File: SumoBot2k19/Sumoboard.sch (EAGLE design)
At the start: 38 parts

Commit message: rerouting
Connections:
- removed net VDD: FL_TOF.7, FR_TOF.7, F_TOF.7, L_TOF.7, R_TOF.7
- net FR_REF: now also B1.A1/15; no longer B1.A6/20*
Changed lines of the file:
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@@
-</segment>
-</net>
-<net name="VDD" class="0">
-<segment>
-<pinref part="L_TOF" gate="G$1" pin="7"/>
-<junction x="2.54" y="20.32"/>
-<label x="2.54" y="20.32" size="1.778" layer="95"/>
-</segment>
-<segment>
-<pinref part="FL_TOF" gate="G$1" pin="7"/>
-<junction x="30.48" y="20.32"/>
-<label x="30.48" y="20.32" size="1.778" layer="95"/>
-</segment>
-<segment>
-<pinref part="F_TOF" gate="G$1" pin="7"/>
-<junction x="58.42" y="20.32"/>
-<label x="58.42" y="20.32" size="1.778" layer="95"/>
-</segment>
-<segment>
-<pinref part="FR_TOF" gate="G$1" pin="7"/>
-<junction x="93.98" y="20.32"/>
-<label x="93.98" y="20.32" size="1.778" layer="95"/>
-</segment>
-<segment>
-<pinref part="R_TOF" gate="G$1" pin="7"/>
-<junction x="121.92" y="20.32"/>
-<label x="121.92" y="20.32" size="1.778" layer="95"/>
 </segment>
 </net>
@@
 <net name="FR_REF" class="0">
 <segment>
-<pinref part="B1" gate="G$1" pin="A6/20*"/>
-<junction x="-2.54" y="86.36"/>
-<label x="-12.7" y="86.36" size="1.778" layer="95"/>
-<wire x1="-12.7" y1="86.36" x2="-2.54" y2="86.36" width="0.1524" layer="91"/>
-</segment>
-<segment>
 <pinref part="FR_REF" gate="J$1" pin="3"/>
 <junction x="149.86" y="106.68"/>
 <label x="149.86" y="106.68" size="1.778" layer="95"/>
 </segment>
+<segment>
+<pinref part="B1" gate="G$1" pin="A1/15"/>
+<junction x="-2.54" y="99.06"/>
+<label x="-12.7" y="99.06" size="1.778" layer="95"/>
+<wire x1="-2.54" y1="99.06" x2="-15.24" y2="99.06" width="0.1524" layer="91"/>
+</segment>
 </net>

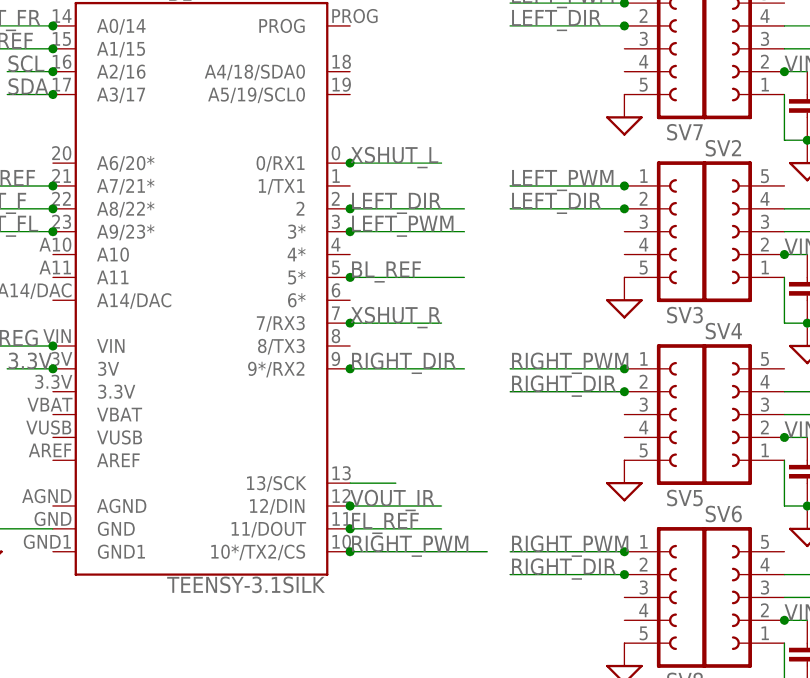
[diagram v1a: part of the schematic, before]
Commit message: added more routes
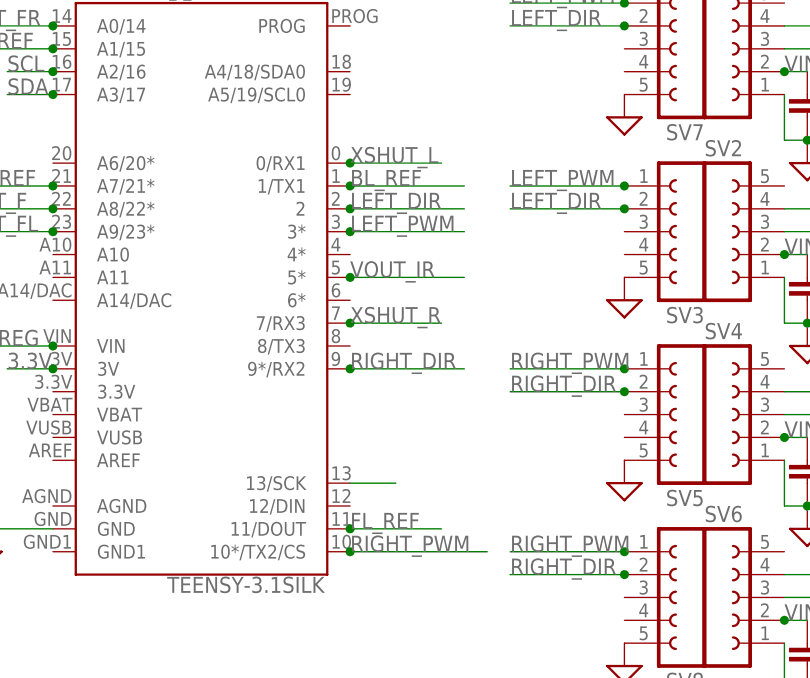
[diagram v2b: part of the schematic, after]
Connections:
- net BL_REF: now also B1.1/TX1; no longer B1.5*
- net VOUT_IR: now also B1.5*; no longer B1.12/DIN
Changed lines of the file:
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@@
 </segment>
 <segment>
-<pinref part="B1" gate="G$1" pin="5*"/>
-<junction x="30.48" y="73.66"/>
-<label x="30.48" y="73.66" size="1.778" layer="95"/>
-<wire x1="30.48" y1="73.66" x2="43.18" y2="73.66" width="0.1524" layer="91"/>
+<pinref part="B1" gate="G$1" pin="1/TX1"/>
+<junction x="30.48" y="83.82"/>
+<wire x1="30.48" y1="83.82" x2="43.18" y2="83.82" width="0.1524" layer="91"/>
+<label x="30.48" y="83.82" size="1.778" layer="95"/>
 </segment>
 </net>
@@
 </segment>
 <segment>
-<pinref part="B1" gate="G$1" pin="12/DIN"/>
-<junction x="30.48" y="48.26"/>
-<label x="30.48" y="48.26" size="1.778" layer="95"/>
-<wire x1="40.64" y1="48.26" x2="30.48" y2="48.26" width="0.1524" layer="91"/>
+<pinref part="B1" gate="G$1" pin="5*"/>
+<junction x="30.48" y="73.66"/>
+<wire x1="30.48" y1="73.66" x2="43.18" y2="73.66" width="0.1524" layer="91"/>
+<label x="30.48" y="73.66" size="1.778" layer="95"/>
 </segment>
 </net>

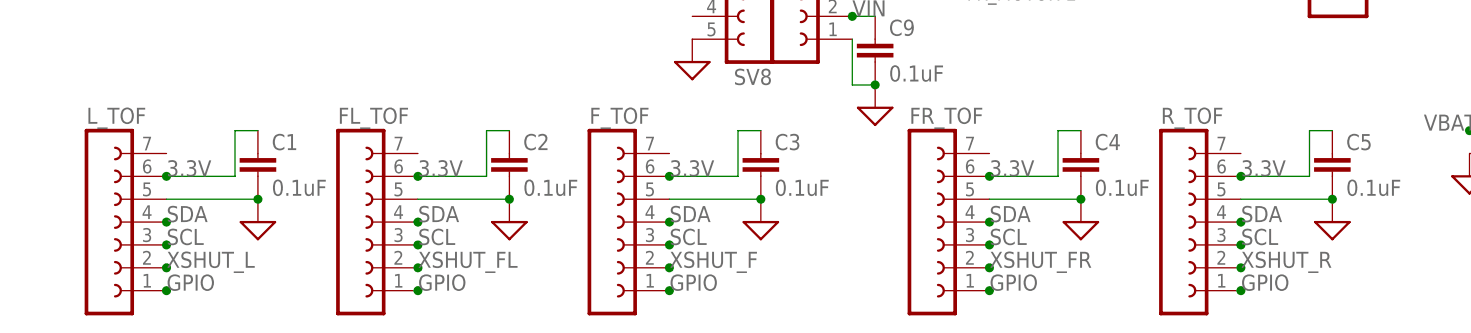
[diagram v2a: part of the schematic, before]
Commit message: need to check battery connection
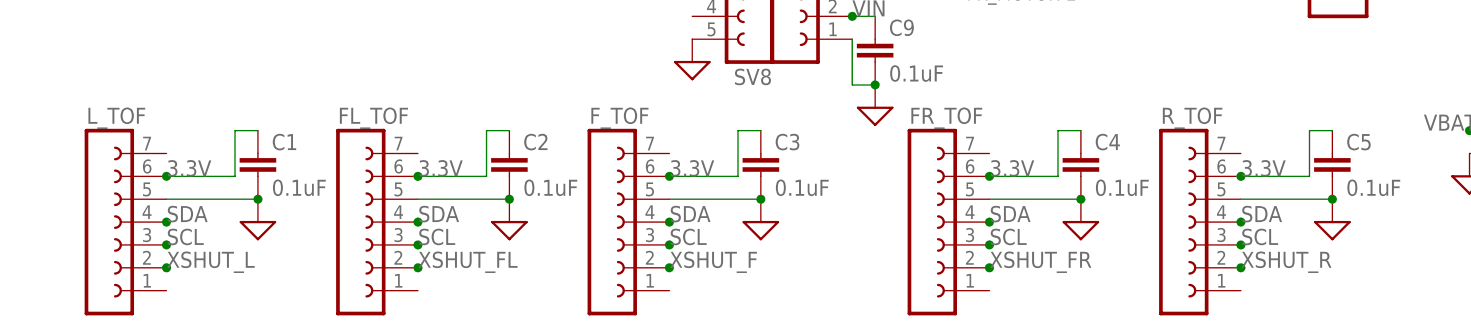
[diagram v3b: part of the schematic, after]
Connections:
- removed net GPIO: FL_TOF.1, FR_TOF.1, F_TOF.1, L_TOF.1, R_TOF.1
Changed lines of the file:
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@@
-</segment>
-</net>
-<net name="GPIO" class="0">
-<segment>
-<pinref part="L_TOF" gate="G$1" pin="1"/>
-<junction x="2.54" y="5.08"/>
-<label x="2.54" y="5.08" size="1.778" layer="95"/>
-</segment>
-<segment>
-<pinref part="FL_TOF" gate="G$1" pin="1"/>
-<junction x="30.48" y="5.08"/>
-<label x="30.48" y="5.08" size="1.778" layer="95"/>
-</segment>
-<segment>
-<pinref part="F_TOF" gate="G$1" pin="1"/>
-<junction x="58.42" y="5.08"/>
-<label x="58.42" y="5.08" size="1.778" layer="95"/>
-</segment>
-<segment>
-<pinref part="FR_TOF" gate="G$1" pin="1"/>
-<junction x="93.98" y="5.08"/>
-<label x="93.98" y="5.08" size="1.778" layer="95"/>
-</segment>
-<segment>
-<pinref part="R_TOF" gate="G$1" pin="1"/>
-<junction x="121.92" y="5.08"/>
-<label x="121.92" y="5.08" size="1.778" layer="95"/>
 </segment>
 </net>

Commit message: added rats nest
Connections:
- net VBAT renamed BAT
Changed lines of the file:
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@@
-</segment>
-</net>
-<net name="VBAT" class="0">
-<segment>
-<pinref part="SWITCH" gate="J$1" pin="1"/>
-<junction x="139.7" y="38.1"/>
-<label x="139.7" y="38.1" size="1.778" layer="95"/>
-</segment>
-<segment>
-<pinref part="BATTERY" gate="-1" pin="S"/>
-<junction x="147.32" y="22.86"/>
-<label x="142.24" y="22.86" size="1.778" layer="95"/>
 </segment>
 </net>
@@
 </segment>
 </net>
+<net name="BAT" class="0">
+<segment>
+<pinref part="BATTERY" gate="-1" pin="S"/>
+<junction x="147.32" y="22.86"/>
+<label x="142.24" y="22.86" size="1.778" layer="95"/>
+</segment>
+<segment>
+<pinref part="SWITCH" gate="J$1" pin="1"/>
+<junction x="139.7" y="38.1"/>
+<label x="139.7" y="38.1" size="1.778" layer="95"/>
+<wire x1="139.7" y1="38.1" x2="147.32" y2="38.1" width="0.1524" layer="91"/>
+</segment>
+</net>
